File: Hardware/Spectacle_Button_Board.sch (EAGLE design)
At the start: 48 parts, among them J17 AUDIO-JACK3, J19 FTDI_DEVICE, J20 AUDIO-JACK3, U1 CY8C4146LQI-S422, U2 3.3V/150mA

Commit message: Final for review
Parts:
- added FD1, FD2: FIDUCIALUFIDUCIAL, SparkFun-Aesthetics:FIDUCIALUFIDUCIAL
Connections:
- net SDA: now also J20.RING1, J20.TIP
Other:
- note added: "VIN 4-6V"
- moved on the sheet: J17, J20
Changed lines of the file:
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@@
 <part name="LOGO1" library="SparkFun-Aesthetics" deviceset="OSHW-LOGO" device="M"/>
 <part name="LOGO2" library="SparkFun-Aesthetics" deviceset="SFE_LOGO_NAME_FLAME" device=".1_INCH"/>
+<part name="FD1" library="SparkFun-Aesthetics" deviceset="FIDUCIAL" device="UFIDUCIAL"/>
+<part name="FD2" library="SparkFun-Aesthetics" deviceset="FIDUCIAL" device="UFIDUCIAL"/>
 </parts>
 <sheets>
@@
 <text x="165.1" y="7.62" size="2.54" layer="94">Dia Campbell/Mike Hord</text>
 <text x="238.76" y="7.62" size="2.54" layer="94">01</text>
+<text x="2.794" y="95.758" size="1.778" layer="97">VIN 4-6V</text>
 </plain>
 <instances>
@@
 <instance part="U1" gate="G0" x="172.72" y="157.48"/>
 <instance part="U1" gate="G3" x="172.72" y="127"/>
-<instance part="U1" gate="G4" x="10.16" y="144.78"/>
+<instance part="U1" gate="G4" x="10.16" y="144.78" smashed="yes">
+<attribute name="NAME" x="2.54" y="169.926" size="1.27" layer="94"/>
+<attribute name="VALUE" x="2.54" y="168.148" size="1.27" layer="94"/>
+</instance>
 <instance part="GND1" gate="1" x="25.4" y="99.06"/>
 <instance part="SUPPLY2" gate="G$1" x="7.62" y="121.92"/>
@@
 <instance part="C5" gate="G$1" x="17.78" y="109.22"/>
 <instance part="C6" gate="G$1" x="7.62" y="109.22"/>
-<instance part="GND9" gate="1" x="190.5" y="63.5"/>
+<instance part="GND9" gate="1" x="185.42" y="63.5"/>
 <instance part="SUPPLY7" gate="G$1" x="190.5" y="93.98"/>
 <instance part="R3" gate="G$1" x="198.12" y="83.82" rot="R90"/>
@@
 <instance part="R6" gate="G$1" x="226.06" y="162.56" rot="R180"/>
 <instance part="GND15" gate="1" x="38.1" y="132.08"/>
-<instance part="J17" gate="G$1" x="175.26" y="73.66"/>
+<instance part="J17" gate="G$1" x="167.64" y="73.66"/>
 <instance part="D4" gate="G$1" x="208.28" y="58.42"/>
 <instance part="D5" gate="G$1" x="208.28" y="40.64"/>
@@
 <instance part="SUPPLY13" gate="G$1" x="205.74" y="101.6"/>
 <instance part="SUPPLY14" gate="G$1" x="228.6" y="137.16"/>
-<instance part="J20" gate="G$1" x="175.26" y="55.88"/>
-<instance part="GND21" gate="1" x="187.96" y="45.72"/>
+<instance part="J20" gate="G$1" x="167.64" y="53.34"/>
+<instance part="GND21" gate="1" x="185.42" y="43.18"/>
 <instance part="LOGO1" gate="G$1" x="127" y="15.24"/>
 <instance part="LOGO2" gate="G$1" x="50.8" y="0"/>
+<instance part="FD1" gate="G$1" x="243.84" y="33.02"/>
+<instance part="FD2" gate="G$1" x="243.84" y="25.4"/>
 </instances>
 <busses>
@@
 <pinref part="J17" gate="G$1" pin="RING2"/>
 <pinref part="GND9" gate="1" pin="GND"/>
-<wire x1="180.34" y1="68.58" x2="190.5" y2="68.58" width="0.1524" layer="91"/>
-<wire x1="190.5" y1="68.58" x2="190.5" y2="66.04" width="0.1524" layer="91"/>
+<wire x1="172.72" y1="68.58" x2="185.42" y2="68.58" width="0.1524" layer="91"/>
+<wire x1="185.42" y1="68.58" x2="185.42" y2="66.04" width="0.1524" layer="91"/>
 </segment>
 <segment>
@@
 <pinref part="J20" gate="G$1" pin="RING2"/>
 <pinref part="GND21" gate="1" pin="GND"/>
-<wire x1="180.34" y1="50.8" x2="187.96" y2="50.8" width="0.1524" layer="91"/>
-<wire x1="187.96" y1="50.8" x2="187.96" y2="48.26" width="0.1524" layer="91"/>
+<wire x1="172.72" y1="48.26" x2="185.42" y2="48.26" width="0.1524" layer="91"/>
+<wire x1="185.42" y1="48.26" x2="185.42" y2="45.72" width="0.1524" layer="91"/>
 </segment>
 </net>
@@
 <pinref part="J17" gate="G$1" pin="EARTH"/>
 <wire x1="190.5" y1="78.74" x2="190.5" y2="93.98" width="0.1524" layer="91"/>
-<wire x1="180.34" y1="78.74" x2="190.5" y2="78.74" width="0.1524" layer="91"/>
+<wire x1="172.72" y1="78.74" x2="190.5" y2="78.74" width="0.1524" layer="91"/>
 <wire x1="190.5" y1="78.74" x2="195.58" y2="78.74" width="0.1524" layer="91"/>
 <junction x="190.5" y="78.74"/>
@@
 <wire x1="195.58" y1="48.26" x2="203.2" y2="48.26" width="0.1524" layer="91"/>
 <pinref part="J20" gate="G$1" pin="EARTH"/>
-<wire x1="180.34" y1="60.96" x2="185.42" y2="60.96" width="0.1524" layer="91"/>
-<wire x1="185.42" y1="60.96" x2="185.42" y2="58.42" width="0.1524" layer="91"/>
-<wire x1="185.42" y1="58.42" x2="195.58" y2="58.42" width="0.1524" layer="91"/>
+<wire x1="172.72" y1="58.42" x2="195.58" y2="58.42" width="0.1524" layer="91"/>
 <junction x="195.58" y="58.42"/>
 </segment>
@@
 <pinref part="R3" gate="G$1" pin="1"/>
 <wire x1="198.12" y1="78.74" x2="198.12" y2="76.2" width="0.1524" layer="91"/>
-<wire x1="198.12" y1="76.2" x2="180.34" y2="76.2" width="0.1524" layer="91"/>
+<wire x1="198.12" y1="76.2" x2="172.72" y2="76.2" width="0.1524" layer="91"/>
 <wire x1="198.12" y1="76.2" x2="200.66" y2="76.2" width="0.1524" layer="91"/>
 <junction x="198.12" y="76.2"/>
@@
 <wire x1="213.36" y1="78.74" x2="213.36" y2="73.66" width="0.1524" layer="91"/>
 <wire x1="213.36" y1="73.66" x2="198.12" y2="73.66" width="0.1524" layer="91"/>
-<wire x1="198.12" y1="73.66" x2="185.42" y2="73.66" width="0.1524" layer="91"/>
+<wire x1="198.12" y1="73.66" x2="193.04" y2="73.66" width="0.1524" layer="91"/>
+<wire x1="193.04" y1="73.66" x2="190.5" y2="73.66" width="0.1524" layer="91"/>
+<wire x1="190.5" y1="73.66" x2="185.42" y2="73.66" width="0.1524" layer="91"/>
 <wire x1="213.36" y1="73.66" x2="215.9" y2="73.66" width="0.1524" layer="91"/>
 <junction x="213.36" y="73.66"/>
 <label x="215.9" y="73.66" size="1.27" layer="95" xref="yes"/>
 <pinref part="J17" gate="G$1" pin="TIP"/>
-<wire x1="180.34" y1="71.12" x2="185.42" y2="71.12" width="0.1524" layer="91"/>
+<wire x1="172.72" y1="71.12" x2="185.42" y2="71.12" width="0.1524" layer="91"/>
 <wire x1="185.42" y1="71.12" x2="185.42" y2="73.66" width="0.1524" layer="91"/>
 <pinref part="D4" gate="G$1" pin="2"/>
@@
 <wire x1="198.12" y1="60.96" x2="198.12" y2="73.66" width="0.1524" layer="91"/>
 <junction x="198.12" y="73.66"/>
-</segment>
-<segment>
+<pinref part="J20" gate="G$1" pin="TIP"/>
+<wire x1="172.72" y1="50.8" x2="193.04" y2="50.8" width="0.1524" layer="91"/>
+<wire x1="193.04" y1="50.8" x2="193.04" y2="73.66" width="0.1524" layer="91"/>
+<junction x="193.04" y="73.66"/>
+<pinref part="J20" gate="G$1" pin="RING1"/>
+<wire x1="172.72" y1="55.88" x2="190.5" y2="55.88" width="0.1524" layer="91"/>
+<wire x1="190.5" y1="55.88" x2="190.5" y2="73.66" width="0.1524" layer="91"/>
+<junction x="190.5" y="73.66"/>
+</segment>
+<segment>

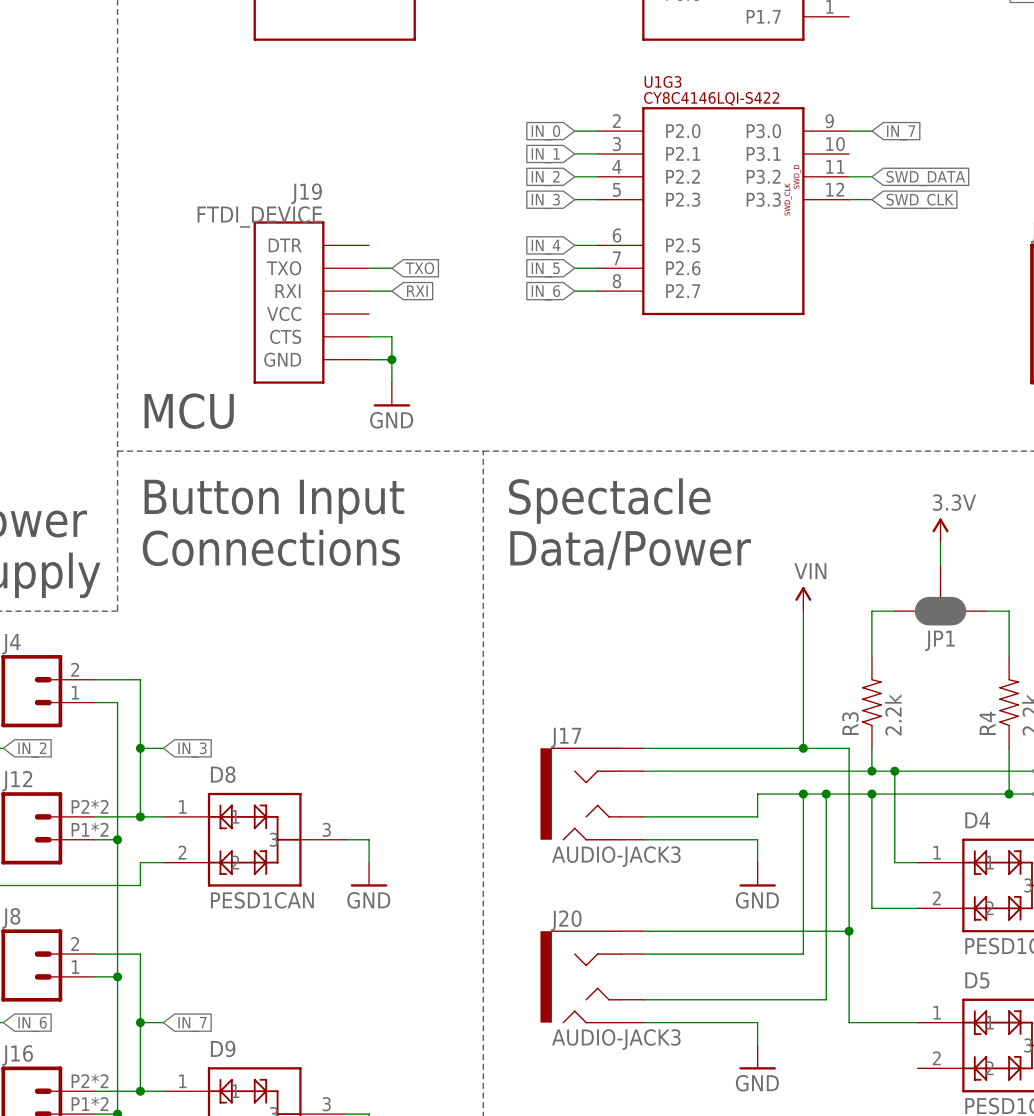
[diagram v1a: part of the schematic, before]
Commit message: added staking vias, straightened headers
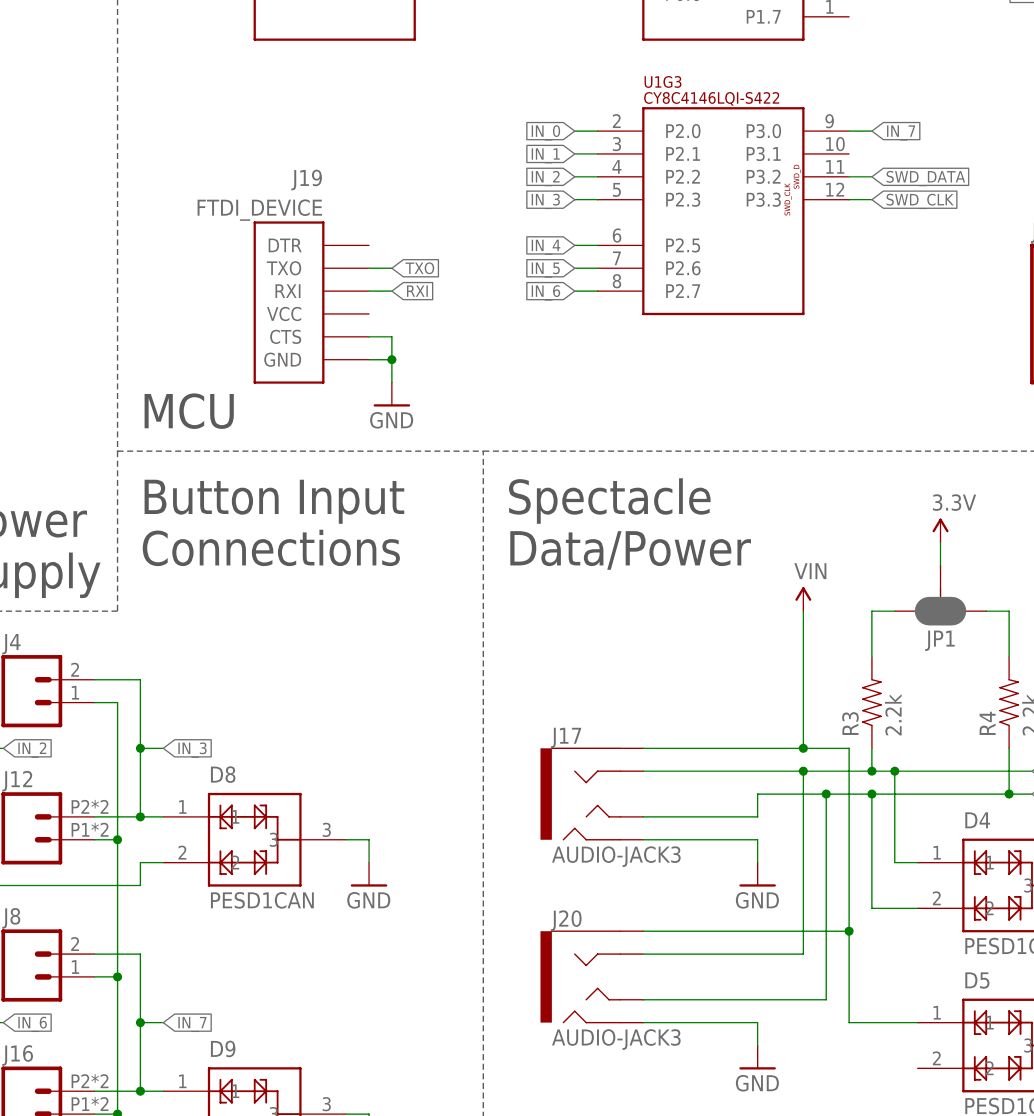
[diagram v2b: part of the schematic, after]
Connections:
- net SCL: now also J20.RING1
- net SDA: no longer J20.RING1
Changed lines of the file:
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@@
 <?xml version="1.0" encoding="utf-8"?>
 <!DOCTYPE eagle SYSTEM "eagle.dtd">
-<eagle version="7.6.0">
+<eagle version="7.3.0">
 <drawing>
 <settings>
@@
 <layer number="255" name="routoute" color="7" fill="1" visible="yes" active="yes"/>
 </layers>
-<schematic xreflabel="%F%N/%S" xrefpart="1_/%S.%C%R">
+<schematic xreflabel="%F%N/%S" xrefpart="/%S.%C%R">
 <attributes>
 </attributes>
@@
 <instance part="J18" gate="G$1" x="218.44" y="127"/>
 <instance part="GND10" gate="1" x="233.68" y="116.84"/>
-<instance part="J19" gate="G$1" x="137.16" y="129.54" rot="MR0"/>
+<instance part="J19" gate="G$1" x="137.16" y="129.54" smashed="yes" rot="MR0">
+<attribute name="NAME" x="137.16" y="141.224" size="1.778" layer="95" rot="MR0"/>
+<attribute name="VALUE" x="137.16" y="137.922" size="1.778" layer="96" rot="MR0"/>
+</instance>
 <instance part="GND11" gate="1" x="144.78" y="116.84"/>
 <instance part="D2" gate="G$1" x="86.36" y="157.48"/>
@@
 <pinref part="R3" gate="G$1" pin="1"/>
 <wire x1="198.12" y1="78.74" x2="198.12" y2="76.2" width="0.1524" layer="91"/>
-<wire x1="198.12" y1="76.2" x2="172.72" y2="76.2" width="0.1524" layer="91"/>
+<wire x1="198.12" y1="76.2" x2="190.5" y2="76.2" width="0.1524" layer="91"/>
+<wire x1="190.5" y1="76.2" x2="172.72" y2="76.2" width="0.1524" layer="91"/>
 <wire x1="198.12" y1="76.2" x2="200.66" y2="76.2" width="0.1524" layer="91"/>
 <junction x="198.12" y="76.2"/>
@@
 <wire x1="200.66" y1="66.04" x2="200.66" y2="76.2" width="0.1524" layer="91"/>
 <junction x="200.66" y="76.2"/>
+<pinref part="J20" gate="G$1" pin="RING1"/>
+<wire x1="172.72" y1="55.88" x2="190.5" y2="55.88" width="0.1524" layer="91"/>
+<wire x1="190.5" y1="55.88" x2="190.5" y2="76.2" width="0.1524" layer="91"/>
+<junction x="190.5" y="76.2"/>
 </segment>
 <segment>
@@
 <wire x1="213.36" y1="73.66" x2="198.12" y2="73.66" width="0.1524" layer="91"/>
 <wire x1="198.12" y1="73.66" x2="193.04" y2="73.66" width="0.1524" layer="91"/>
-<wire x1="193.04" y1="73.66" x2="190.5" y2="73.66" width="0.1524" layer="91"/>
-<wire x1="190.5" y1="73.66" x2="185.42" y2="73.66" width="0.1524" layer="91"/>
+<wire x1="193.04" y1="73.66" x2="185.42" y2="73.66" width="0.1524" layer="91"/>
 <wire x1="213.36" y1="73.66" x2="215.9" y2="73.66" width="0.1524" layer="91"/>
 <junction x="213.36" y="73.66"/>
@@
 <wire x1="193.04" y1="50.8" x2="193.04" y2="73.66" width="0.1524" layer="91"/>
 <junction x="193.04" y="73.66"/>
-<pinref part="J20" gate="G$1" pin="RING1"/>
-<wire x1="172.72" y1="55.88" x2="190.5" y2="55.88" width="0.1524" layer="91"/>
-<wire x1="190.5" y1="55.88" x2="190.5" y2="73.66" width="0.1524" layer="91"/>
-<junction x="190.5" y="73.66"/>
-</segment>
-<segment>
+</segment>
+<segment>
